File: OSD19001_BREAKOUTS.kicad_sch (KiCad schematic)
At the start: 139 parts, among them J2 ${PARTNUMBER}, U1 ${PARTNUMBER}

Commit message: Converted ref des (annotation) to Kicad style: PA01 => PA1, etc, for all P[ABCD]0[1-9] PTXD => PTXD1 PRXD => PRXD1 PGND => PGND1
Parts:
- renumbered PA01 to PA1, PA02 to PA2, PA03 to PA3, PA04 to PA4, PA05 to PA5, PA06 to PA6, PA07 to PA7, PA08 to PA8, PA09 to PA9, PB01 to PB1, PB02 to PB2, PB03 to PB3, PB04 to PB4, PB05 to PB5, PB06 to PB6, PB07 to PB7, PB08 to PB8, PB09 to PB9, PC01 to PC1, PC02 to PC2, PC03 to PC3, PC04 to PC4, PC05 to PC5, PC06 to PC6, PC07 to PC7, PC08 to PC8, PC09 to PC9, PD01 to PD1, PD02 to PD2, PD03 to PD3, PD04 to PD4, PD05 to PD5, PD06 to PD6, PD07 to PD7, PD08 to PD8, PD09 to PD9, PGND to PGND1, PRXD to PRXD1, PTXD to PTXD1

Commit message: Added PWR FLAGS. Passes ERC, no errors or warnings
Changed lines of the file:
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@@
     (stroke (width 0.254) (type solid) (color 0 0 0 0))
+  )
+  (wire (pts (xy 227.33 168.91) (xy 236.22 168.91))
+    (stroke (width 0) (type solid) (color 0 0 0 0))
+  )
+  (wire (pts (xy 227.33 176.53) (xy 236.22 176.53))
+    (stroke (width 0) (type solid) (color 0 0 0 0))
+  )
+  (wire (pts (xy 227.33 182.88) (xy 236.22 182.88))
+    (stroke (width 0) (type solid) (color 0 0 0 0))
+  )
+  (wire (pts (xy 234.95 189.23) (xy 227.33 189.23))
+    (stroke (width 0) (type solid) (color 0 0 0 0))
   )
   (wire (pts (xy 238.76 86.36) (xy 241.3 86.36))
@@
     (effects (font (size 1.27 1.27)) (justify right))
   )
+  (symbol (lib_id "power:PWR_FLAG") (at 234.95 189.23 0) (mirror y) (unit 1)
+    (in_bom yes) (on_board yes) (fields_autoplaced)
+    (property "Reference" "#FLG0101" (id 0) (at 234.95 187.325 0)
+      (effects (font (size 1.27 1.27)) hide)
+    )
+    (property "Value" "PWR_FLAG" (id 1) (at 234.95 184.15 0))
+    (property "Footprint" "" (id 2) (at 234.95 189.23 0)
+      (effects (font (size 1.27 1.27)) hide)
+    )
+    (property "Datasheet" "~" (id 3) (at 234.95 189.23 0)
+      (effects (font (size 1.27 1.27)) hide)
+    )
+    (pin "1")
+  )
+  (symbol (lib_id "power:PWR_FLAG") (at 236.22 168.91 0) (unit 1)
+    (in_bom yes) (on_board yes) (fields_autoplaced)
+    (property "Reference" "#FLG0102" (id 0) (at 236.22 167.005 0)
+      (effects (font (size 1.27 1.27)) hide)
+    )
+    (property "Value" "PWR_FLAG" (id 1) (at 236.22 163.83 0))
+    (property "Footprint" "" (id 2) (at 236.22 168.91 0)
+      (effects (font (size 1.27 1.27)) hide)
+    )
+    (property "Datasheet" "~" (id 3) (at 236.22 168.91 0)
+      (effects (font (size 1.27 1.27)) hide)
+    )
+    (pin "1")
+  )
+  (symbol (lib_id "power:PWR_FLAG") (at 236.22 176.53 0) (unit 1)
+    (in_bom yes) (on_board yes) (fields_autoplaced)
+    (property "Reference" "#FLG0103" (id 0) (at 236.22 174.625 0)
+      (effects (font (size 1.27 1.27)) hide)
+    )
+    (property "Value" "PWR_FLAG" (id 1) (at 236.22 171.45 0))
+    (property "Footprint" "" (id 2) (at 236.22 176.53 0)
+      (effects (font (size 1.27 1.27)) hide)
+    )
+    (property "Datasheet" "~" (id 3) (at 236.22 176.53 0)
+      (effects (font (size 1.27 1.27)) hide)
+    )
+    (pin "1")
+  )
+  (symbol (lib_id "power:PWR_FLAG") (at 236.22 182.88 0) (unit 1)
+    (in_bom yes) (on_board yes) (fields_autoplaced)
+    (property "Reference" "#FLG0104" (id 0) (at 236.22 180.975 0)
+      (effects (font (size 1.27 1.27)) hide)
+    )
+    (property "Value" "PWR_FLAG" (id 1) (at 236.22 177.8 0))
+    (property "Footprint" "" (id 2) (at 236.22 182.88 0)
+      (effects (font (size 1.27 1.27)) hide)
+    )
+    (property "Datasheet" "~" (id 3) (at 236.22 182.88 0)
+      (effects (font (size 1.27 1.27)) hide)
+    )
+    (pin "1")
+  )
   (symbol (lib_id "OSD19001_BREAKOUTS-altium-import:+3.3V") (at 73.66 182.88 180) (unit 1)
     (in_bom yes) (on_board yes)
@@
       (effects (font (size 1.27 1.27)) hide)
     )
+    (pin "")
+  )
+  (symbol (lib_id "OSD19001_BREAKOUTS-altium-import:+VBST") (at 227.33 168.91 180) (unit 1)
+    (in_bom yes) (on_board yes)
+    (property "Reference" "#PWR0102" (id 0) (at 227.33 168.91 0)
+      (effects (font (size 1.27 1.27)) hide)
+    )
+    (property "Value" "+VBST" (id 1) (at 227.33 165.1 0))
+    (property "Footprint" "" (id 2) (at 227.33 168.91 0)
+      (effects (font (size 1.27 1.27)) hide)
+    )
+    (property "Datasheet" "" (id 3) (at 227.33 168.91 0)
+      (effects (font (size 1.27 1.27)) hide)
+    )
+    (pin "")
+  )
+  (symbol (lib_id "OSD19001_BREAKOUTS-altium-import:+VSW") (at 227.33 176.53 180) (unit 1)
+    (in_bom yes) (on_board yes)
+    (property "Reference" "#PWR0103" (id 0) (at 227.33 176.53 0)
+      (effects (font (size 1.27 1.27)) hide)
+    )
+    (property "Value" "+VSW" (id 1) (at 227.33 172.72 0))
+    (property "Footprint" "" (id 2) (at 227.33 176.53 0)
+      (effects (font (size 1.27 1.27)) hide)
+    )
+    (property "Datasheet" "" (id 3) (at 227.33 176.53 0)
+      (effects (font (size 1.27 1.27)) hide)
+    )
+    (pin "")
+  )
+  (symbol (lib_id "OSD19001_BREAKOUTS-altium-import:+VLDO2") (at 227.33 182.88 180) (unit 1)
+    (in_bom yes) (on_board yes)
+    (property "Reference" "#PWR0104" (id 0) (at 227.33 182.88 0)
+      (effects (font (size 1.27 1.27)) hide)
+    )
+    (property "Value" "+VLDO2" (id 1) (at 227.33 179.07 0))
+    (property "Footprint" "" (id 2) (at 227.33 182.88 0)
+      (effects (font (size 1.27 1.27)) hide)
+    )
+    (property "Datasheet" "" (id 3) (at 227.33 182.88 0)
+      (effects (font (size 1.27 1.27)) hide)
+    )
+    (pin "")
+  )
+  (symbol (lib_id "OSD19001_BREAKOUTS-altium-import:+3.3V") (at 227.33 189.23 0) (mirror x) (unit 1)
+    (in_bom yes) (on_board yes)
+    (property "Reference" "#PWR0101" (id 0) (at 227.33 189.23 0)
+      (effects (font (size 1.27 1.27)) hide)
+    )
+    (property "Value" "+3.3V" (id 1) (at 227.33 185.42 0))
+    (property "Footprint" "" (id 2) (at 227.33 189.23 0)
+      (effects (font (size 1.27 1.27)) hide)
+    )
+    (property "Datasheet" "" (id 3) (at 227.33 189.23 0)
+      (effects (font (size 1.27 1.27)) hide)
+    )

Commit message: Fixed schematic symbol values: were set to Altium variables
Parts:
- D1, D2: value ${PARTNUMBER} -> 150066SV74000
- J2: value ${PARTNUMBER} -> 104031-0811
- R1, R2, R3, R4, R5, R6: value ${ALTIUM_VALUE} -> 10K
- R10, R11, R12, R9: value ${ALTIUM_VALUE} -> 330
- U1: value ${PARTNUMBER} -> OSD32MP157C-512M-BAA
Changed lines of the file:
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@@
       (effects (font (size 1.27 1.27)) (justify left bottom))
     )
-    (property "Value" "${ALTIUM_VALUE}" (id 1) (at 68.072 185.42 0)
+    (property "Value" "10K" (id 1) (at 68.072 185.42 0)
       (effects (font (size 1.27 1.27)) (justify left bottom))
     )
@@
       (effects (font (size 1.27 1.27)) (justify left bottom))
     )
-    (property "Value" "${ALTIUM_VALUE}" (id 1) (at 68.072 187.96 0)
+    (property "Value" "10K" (id 1) (at 68.072 187.96 0)
       (effects (font (size 1.27 1.27)) (justify left bottom))
     )
@@
       (effects (font (size 1.27 1.27)) (justify left bottom))
     )
-    (property "Value" "${ALTIUM_VALUE}" (id 1) (at 68.072 190.5 0)
+    (property "Value" "10K" (id 1) (at 68.072 190.5 0)
       (effects (font (size 1.27 1.27)) (justify left bottom))
     )
@@
       (effects (font (size 1.27 1.27)) (justify left bottom))
     )
-    (property "Value" "${ALTIUM_VALUE}" (id 1) (at 68.072 193.04 0)
+    (property "Value" "10K" (id 1) (at 68.072 193.04 0)
       (effects (font (size 1.27 1.27)) (justify left bottom))
     )
@@
       (effects (font (size 1.27 1.27)) (justify left bottom))
     )
-    (property "Value" "${ALTIUM_VALUE}" (id 1) (at 68.072 195.58 0)
+    (property "Value" "10K" (id 1) (at 68.072 195.58 0)
       (effects (font (size 1.27 1.27)) (justify left bottom))
     )
@@
       (effects (font (size 1.27 1.27)) (justify left bottom))
     )
-    (property "Value" "${ALTIUM_VALUE}" (id 1) (at 67.818 223.52 0)
+    (property "Value" "10K" (id 1) (at 67.818 223.52 0)
       (effects (font (size 1.27 1.27)) (justify left bottom))
     )
@@
       (effects (font (size 1.27 1.27)) (justify left bottom))
     )
-    (property "Value" "${ALTIUM_VALUE}" (id 1) (at 203.962 85.598 0)
+    (property "Value" "330" (id 1) (at 203.962 85.598 0)
       (effects (font (size 1.27 1.27)) (justify left bottom))
     )
@@
       (effects (font (size 1.27 1.27)) (justify left bottom))
     )
-    (property "Value" "${ALTIUM_VALUE}" (id 1) (at 203.962 93.218 0)
+    (property "Value" "330" (id 1) (at 203.962 93.218 0)
       (effects (font (size 1.27 1.27)) (justify left bottom))
     )
@@
       (effects (font (size 1.27 1.27)) (justify left bottom))
     )
-    (property "Value" "${ALTIUM_VALUE}" (id 1) (at 203.962 138.938 0)
+    (property "Value" "330" (id 1) (at 203.962 138.938 0)
       (effects (font (size 1.27 1.27)) (justify left bottom))
     )
@@
       (effects (font (size 1.27 1.27)) (justify left bottom))
     )
-    (property "Value" "${ALTIUM_VALUE}" (id 1) (at 203.962 146.558 0)
+    (property "Value" "330" (id 1) (at 203.962 146.558 0)
       (effects (font (size 1.27 1.27)) (justify left bottom))
     )
@@
       (effects (font (size 1.27 1.27)) (justify left bottom))
     )
-    (property "Value" "${PARTNUMBER}" (id 1) (at 219.202 81.28 0)
+    (property "Value" "150066SV74000" (id 1) (at 219.202 81.28 0)
       (effects (font (size 1.27 1.27)) (justify left bottom))
     )
@@
       (effects (font (size 1.27 1.27)) (justify left bottom))
     )
-    (property "Value" "${PARTNUMBER}" (id 1) (at 219.202 134.62 0)
+    (property "Value" "150066SV74000" (id 1) (at 219.202 134.62 0)
       (effects (font (size 1.27 1.27)) (justify left bottom))
     )
@@
       (effects (font (size 1.27 1.27)) (justify left bottom))
     )
-    (property "Value" "${PARTNUMBER}" (id 1) (at 175.26 233.68 0)
+    (property "Value" "104031-0811" (id 1) (at 175.26 233.68 0)
       (effects (font (size 1.27 1.27)) (justify left bottom))
     )
@@
       (effects (font (size 1.27 1.27)) (justify left bottom))
     )
-    (property "Value" "${PARTNUMBER}" (id 1) (at 152.4 162.56 0)
+    (property "Value" "OSD32MP157C-512M-BAA" (id 1) (at 152.4 162.56 0)
       (effects (font (size 1.27 1.27)) (justify left bottom))
     )
@@
       (effects (font (size 1.27 1.27)) (justify left bottom))
     )
-    (property "Value" "${PARTNUMBER}" (id 1) (at 37.846 55.88 0)
+    (property "Value" "OSD32MP157C-512M-BAA" (id 1) (at 37.846 55.88 0)
       (effects (font (size 1.27 1.27)) (justify right bottom))
     )
@@
       (effects (font (size 1.27 1.27)) (justify left bottom))
     )
-    (property "Value" "${PARTNUMBER}" (id 1) (at 37.846 109.22 0)
+    (property "Value" "OSD32MP157C-512M-BAA" (id 1) (at 37.846 109.22 0)
       (effects (font (size 1.27 1.27)) (justify right bottom))
     )
@@
       (effects (font (size 1.27 1.27)) (justify left bottom))
     )
-    (property "Value" "${PARTNUMBER}" (id 1) (at 37.592 162.56 0)
+    (property "Value" "OSD32MP157C-512M-BAA" (id 1) (at 37.592 162.56 0)
       (effects (font (size 1.27 1.27)) (justify right bottom))
     )
@@
       (effects (font (size 1.27 1.27)) (justify left bottom))
     )
-    (property "Value" "${PARTNUMBER}" (id 1) (at 37.592 215.9 0)
+    (property "Value" "OSD32MP157C-512M-BAA" (id 1) (at 37.592 215.9 0)
       (effects (font (size 1.27 1.27)) (justify right bottom))
     )
@@
       (effects (font (size 1.27 1.27)) (justify left bottom))
     )
-    (property "Value" "${PARTNUMBER}" (id 1) (at 106.172 55.88 0)
+    (property "Value" "OSD32MP157C-512M-BAA" (id 1) (at 106.172 55.88 0)
       (effects (font (size 1.27 1.27)) (justify right bottom))
     )
@@
       (effects (font (size 1.27 1.27)) (justify left bottom))
     )
-    (property "Value" "${PARTNUMBER}" (id 1) (at 106.172 109.22 0)
+    (property "Value" "OSD32MP157C-512M-BAA" (id 1) (at 106.172 109.22 0)
       (effects (font (size 1.27 1.27)) (justify right bottom))
     )
@@
       (effects (font (size 1.27 1.27)) (justify left bottom))
     )
-    (property "Value" "${PARTNUMBER}" (id 1) (at 106.172 162.56 0)
+    (property "Value" "OSD32MP157C-512M-BAA" (id 1) (at 106.172 162.56 0)
       (effects (font (size 1.27 1.27)) (justify right bottom))
     )
@@
       (effects (font (size 1.27 1.27)) (justify left bottom))
     )
-    (property "Value" "${PARTNUMBER}" (id 1) (at 106.172 215.9 0)
+    (property "Value" "OSD32MP157C-512M-BAA" (id 1) (at 106.172 215.9 0)
       (effects (font (size 1.27 1.27)) (justify right bottom))
     )
@@
       (effects (font (size 1.27 1.27)) (justify left bottom))
     )
-    (property "Value" "${PARTNUMBER}" (id 1) (at 174.752 55.88 0)
+    (property "Value" "OSD32MP157C-512M-BAA" (id 1) (at 174.752 55.88 0)
       (effects (font (size 1.27 1.27)) (justify right bottom))
     )
@@
       (effects (font (size 1.27 1.27)) (justify left bottom))
     )
-    (property "Value" "${PARTNUMBER}" (id 1) (at 174.752 109.22 0)
+    (property "Value" "OSD32MP157C-512M-BAA" (id 1) (at 174.752 109.22 0)
       (effects (font (size 1.27 1.27)) (justify right bottom))
     )

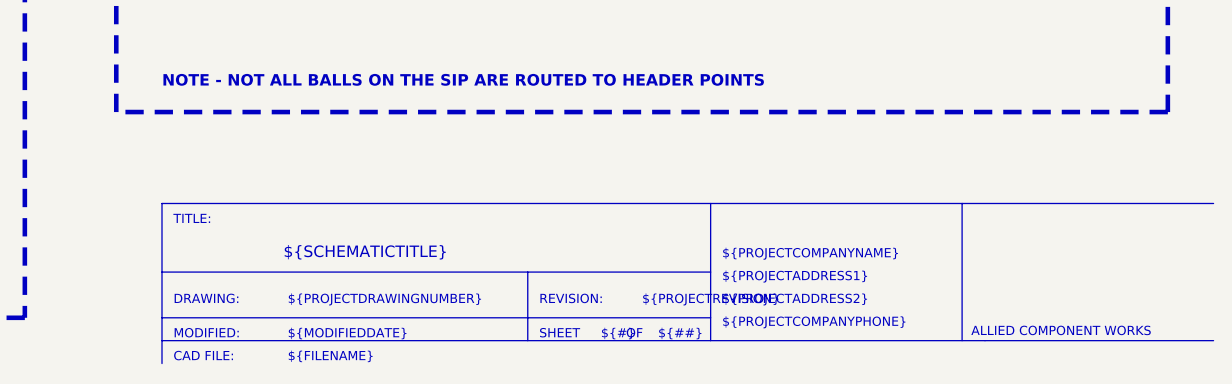
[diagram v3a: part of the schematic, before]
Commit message: Corrected title bar text to match online PDF schematic
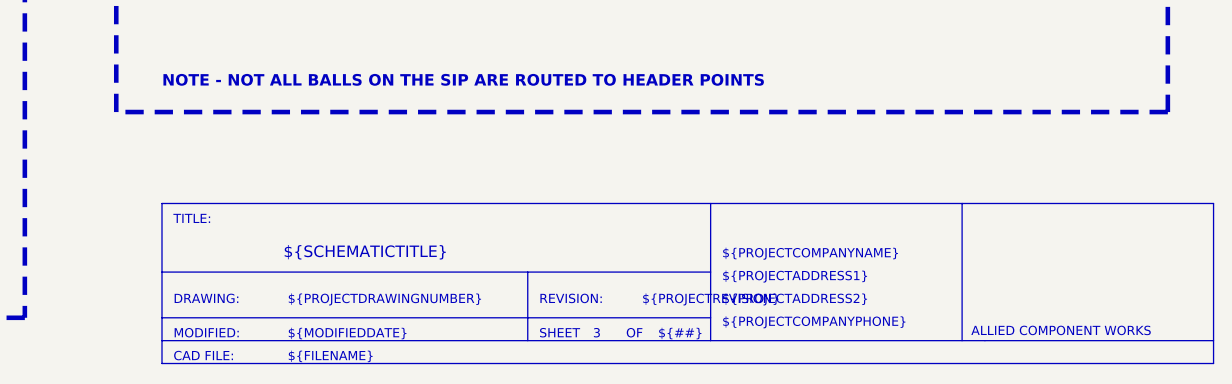
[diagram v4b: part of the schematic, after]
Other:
- note added: "3"
- note removed: "${#}"
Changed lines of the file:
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@@
+    (stroke (width 0) (type solid) (color 0 0 0 0))
+  )
+  (polyline (pts (xy 375.92 256.54) (xy 375.92 274.32))
+    (stroke (width 0) (type solid) (color 0 0 0 0))
+  )
+  (polyline (pts (xy 375.92 274.32) (xy 259.08 274.32))
     (stroke (width 0) (type solid) (color 0 0 0 0))
   )
@@
     (effects (font (size 1.016 1.016)) (justify left bottom))
   )
-  (text "${#}" (at 307.848 271.78 180)
-    (effects (font (size 1.016 1.016)) (justify left bottom))
+  (text "3" (at 307.848 271.78 180)
+    (effects (font (size 1.016 1.016)) (justify right bottom))
   )
   (text "OF" (at 310.642 271.78 180)
